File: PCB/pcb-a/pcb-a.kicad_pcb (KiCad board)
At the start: 2 copper layers, 89.4 x 42.2 mm, 28 parts, among them J1 Conn_02x05_Counter_Clockwise, J2 Conn_02x05_Counter_Clockwise, Q3 BC337, SW1 config, U1 ESP32-S2-DevKitM, U3 L7805

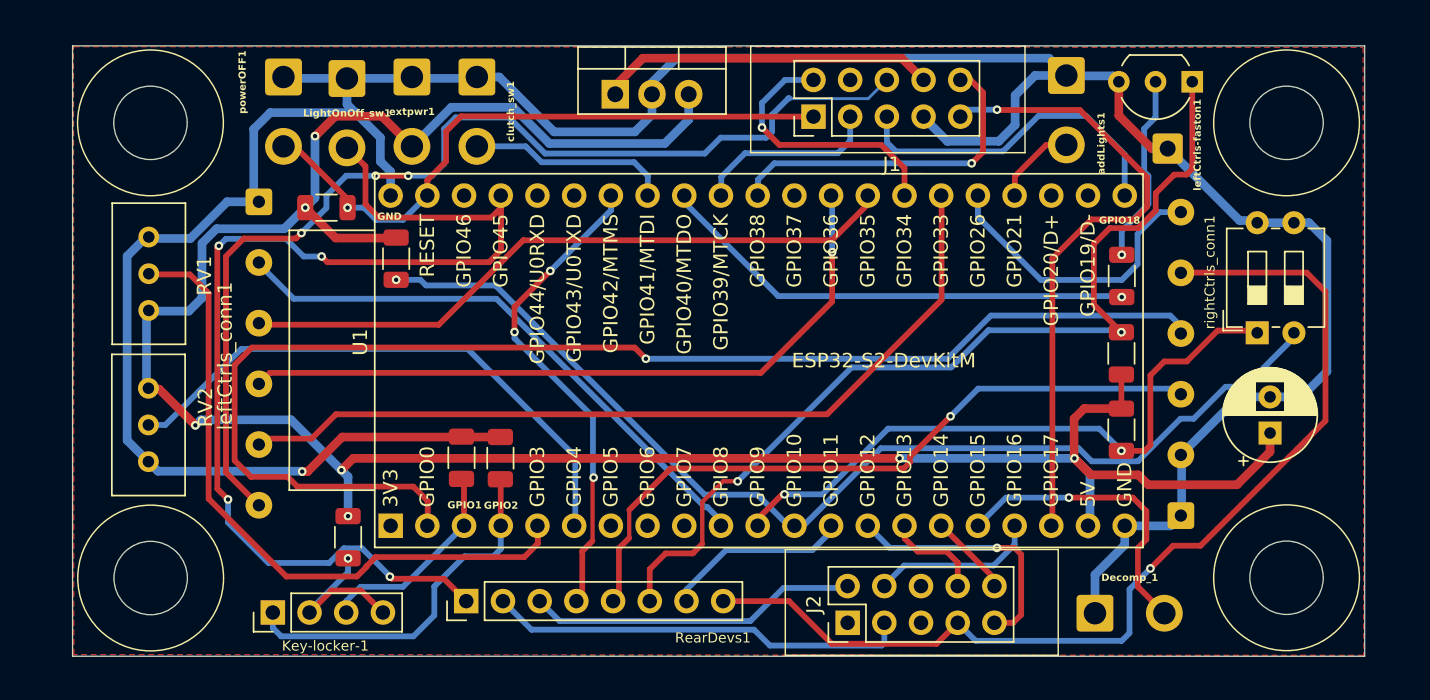
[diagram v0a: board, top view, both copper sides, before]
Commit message: Fixes and changes
- 8pin pin-header connectors have been replaced with more standard 10pin connectors
- Wrong components sizes have been fixed
- too small solder-wire connectors have been fixed
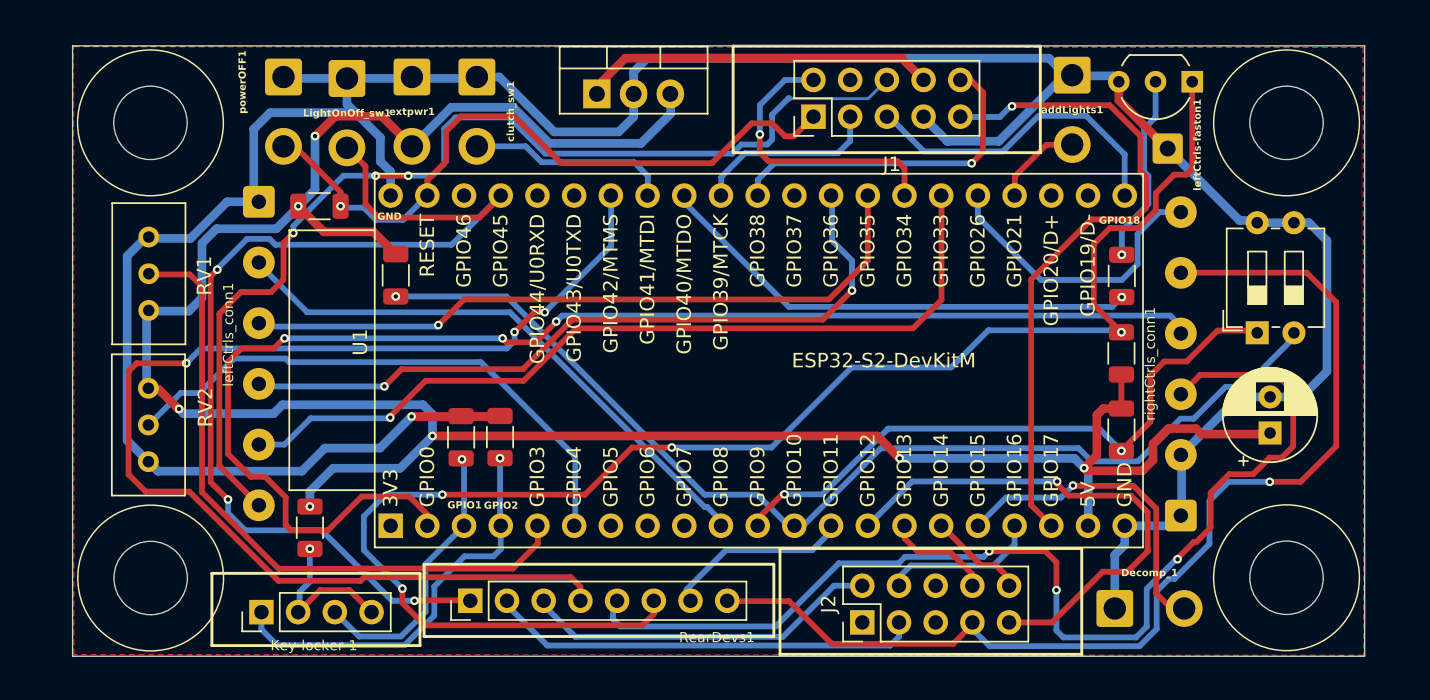
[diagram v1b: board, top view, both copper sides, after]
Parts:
- leftCtrls_conn1, rightCtrls_conn1: footprint Connector_Wire:SolderWire-0.25sqmm_1x06_P4.2mm_D0.65mm_OD1.7mm -> Custom_conn_wire:SolderWire-0.25sqmm_1x06_P4.2mm_D1.0mm_OD2.2mm
- moved R1 2.72 mm to (128.9, 95.5)
- moved R4 1.46 mm to (142.1, 89.2)
- moved R3 1.42 mm to (139.4, 89.2)
- moved Decomp_1 1.41 mm to (184.6, 101.1)
- moved U3 1.27 mm to (148.8, 65.4)
- moved R5 1.15 mm to (134.9, 78.0)
- moved J2 1.02 mm to (167.2, 102.0)
- moved Key-locker-1 0.79 mm to (125.6, 101.3)
- moved R2 0.49 mm to (129.6, 73.2)
- moved addLights1 0.41 mm to (181.7, 64.2)
- moved RearDevs1 0.28 mm to (140.0, 100.5)
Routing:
- net i_bykeStand: track 33.7 -> 83.7 mm
- net c_startEngine: track 66.0 -> 106.8 mm, vias 2 -> 4
- net c_brakeSwitch: track 48.8 -> 77.1 mm, vias 1 -> 3
- net o_keepAlive: track 17.7 -> 36.4 mm
- net i_Vx1: track 14.4 -> 19.7 mm, vias 0 -> 1
- net c_rearLight: track 78.9 -> 73.8 mm, vias 4 -> 3
- net 5V: track 167.3 -> 172.0 mm
- net c_engineOFF: track 71.8 -> 75.8 mm
- net i_powerOFF: track 44.5 -> 48.1 mm
- net i_Vx2: track 25.6 -> 28.5 mm, vias 0 -> 1
- net i_startButton: track 91.0 -> 93.8 mm, vias 1 -> 3
- net o_upLight: track 43.7 -> 46.4 mm
- net i_downLight: track 46.2 -> 48.6 mm, vias 0 -> 1
- net c_rightArrow: track 22.9 -> 24.7 mm
- net i_upLight: track 49.4 -> 51.1 mm, vias 1 -> 2
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
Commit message: hanges and fix
- The R6 and R8 pull-up resistors have been removed. I will use internal ones
- The J2 connector position has been moved
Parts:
- removed R5, R8: 100K, Resistor_SMD:R_1206_3216Metric
- moved Decomp_1 1.46 mm to (185.1, 102.4)
- moved J2 0.38 mm to (167.2, 102.4)
- moved Key-locker-1 0.31 mm to (125.9, 101.3)
- moved RearDevs1 0.25 mm to (140.3, 100.5)
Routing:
- net Net-(U1-GPIO10/TOUCH10/ADC1_CH9/FSPICS0/FSPIIO4): track 75.2 -> 41.7 mm, vias 1 -> 0
- net 5V: track 172.0 -> 163.6 mm
- net c_brakeSwitch: track 77.1 -> 69.1 mm
- net GND: track 206.9 -> 208.5 mm
- net c_engineOFF: track 75.8 -> 74.2 mm, vias 1 -> 2
- net i_decompr: track 23.0 -> 24.2 mm
- net o_keepAlive: track 36.4 -> 37.4 mm
- net Net-(U1-GPIO9/TOUCH9/ADC1_CH8/FSPIHD): track 43.8 -> 42.9 mm, vias 2 -> 0
- net i_Vx2: track 28.5 -> 29.2 mm
- net i_Vx1: track 19.7 -> 20.4 mm
- net c_leftArrow: track 29.8 -> 30.5 mm
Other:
- board size 89.4 x 42.2 mm -> 89.4 x 42.8 mm

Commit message: Small fixes...
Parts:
- moved C1 1.97 mm to (197.3, 89.1)
- moved SW1 1.27 mm to (195.8, 82.0)
- moved rightCtrls_conn1 0.61 mm to (189.8, 94.6)
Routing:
- net c_brakeSwitch: track 69.1 -> 72.9 mm
- net 5V: track 163.6 -> 165.6 mm
- net Net-(U1-GPIO10/TOUCH10/ADC1_CH9/FSPICS0/FSPIIO4): track 41.7 -> 43.3 mm
- net GND: track 208.5 -> 209.6 mm
- net i_engineON: track 20.5 -> 21.1 mm
- net o_keepAlive: track 37.4 -> 36.8 mm
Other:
- board size 89.4 x 42.8 mm -> 89.4 x 43.5 mm

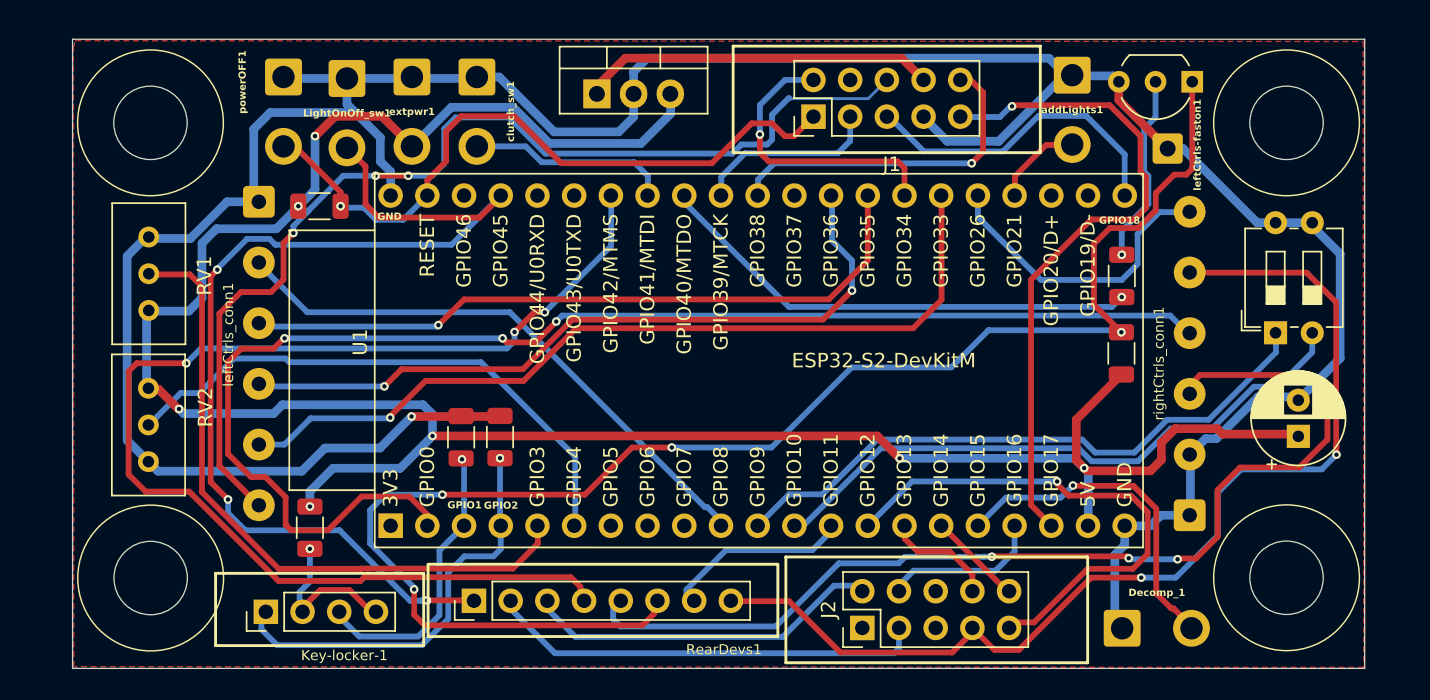
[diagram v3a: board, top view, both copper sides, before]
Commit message: PCBs sizes adjustment to be mounted as totem
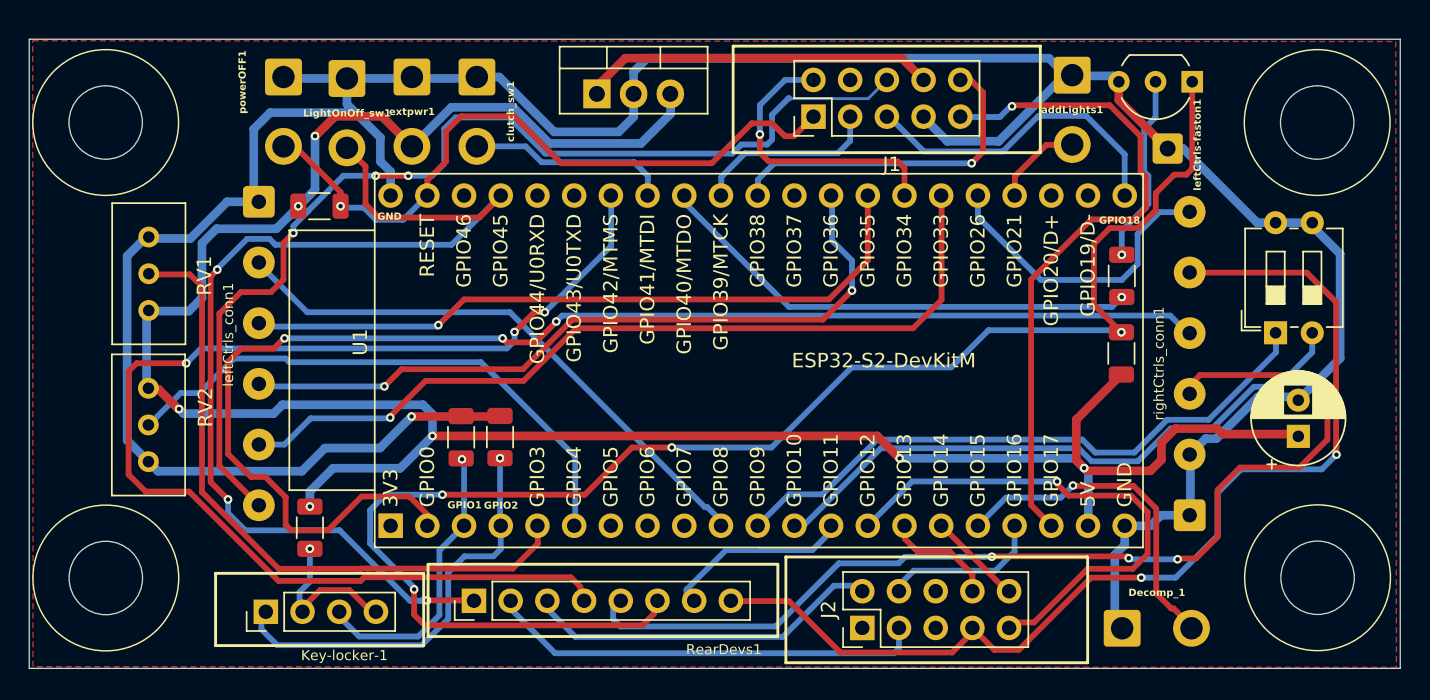
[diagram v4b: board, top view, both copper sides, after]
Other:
- board size 89.4 x 43.5 mm -> 94.9 x 43.5 mm
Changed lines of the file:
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@@
 	)
 	(gr_circle
-		(center 117.906315 67.45)
-		(end 122.95 67.45)
+		(center 114.805085 67.4266)
+		(end 119.84877 67.4266)
 		(stroke
 			(width 0.1)
@@
 	)
 	(gr_circle
-		(center 117.918685 98.95)
-		(end 122.96237 98.95)
+		(center 114.815933 98.947978)
+		(end 119.859618 98.947978)
 		(stroke
 			(width 0.1)
@@
 	)
 	(gr_circle
-		(center 196.524933 67.45)
-		(end 201.568618 67.45)
+		(center 198.646915 67.4266)
+		(end 203.6906 67.4266)
 		(stroke
 			(width 0.1)
@@
 	)
 	(gr_circle
-		(center 196.525 98.931315)
-		(end 201.568685 98.931315)
+		(center 198.672315 98.931315)
+		(end 203.716 98.931315)
 		(stroke
 			(width 0.1)
@@
 	)
 	(gr_circle
-		(center 117.918752 98.95)
-		(end 120.458752 98.939435)
+		(center 114.816 98.947978)
+		(end 117.356 98.937413)
 		(stroke
 			(width 0.05)
@@
 	)
 	(gr_circle
-		(center 196.525067 98.931315)
-		(end 199.065067 98.92075)
+		(center 198.672382 98.931315)
+		(end 201.212382 98.92075)
 		(stroke
 			(width 0.05)
@@
 	)
 	(gr_circle
-		(center 117.906382 67.45)
-		(end 120.446382 67.439435)
+		(center 114.805152 67.4266)
+		(end 117.345152 67.416035)
 		(stroke
 			(width 0.05)
@@
 	)
 	(gr_circle
-		(center 196.525 67.45)
-		(end 199.065 67.439435)
+		(center 198.646982 67.4266)
+		(end 201.186982 67.416035)
 		(stroke
 			(width 0.05)
@@
 	)
 	(gr_rect
-		(start 112.515 61.6648)
-		(end 201.933 105.2022)
+		(start 109.5178 61.6648)
+		(end 204.3968 105.2022)
 		(stroke
 			(width 0.05)
@@
 		(layer "B.Mask")
 		(pts
-			(xy 112.515 62.122) (xy 201.933 62.122)
+			(xy 198.672382 98.931315) (xy 114.816 98.947978)
+		)
+		(height -11.349584)
+		(format
+			(prefix "")
+			(suffix "")
+			(units 3)
+			(units_format 1)
+			(precision 4)
+		)
+		(style
+			(thickness 0.1)
+			(arrow_length 1.27)
+			(text_position_mode 0)
+			(arrow_direction outward)
+			(extension_height 0.58642)
+			(extension_offset 0.5)
+			(keep_text_aligned yes)
+		)
+		(gr_text "83,8564 mm"
+			(at 156.746217 109.139231 0.01138585799)
+			(layer "B.Mask")
+			(effects
+				(font
+					(size 1 1)
+					(thickness 0.15)
+				)
+			)
+		)
+	)
+	(dimension
+		(type aligned)
+		(layer "B.Mask")
+		(pts
+			(xy 109.75368 61.767957) (xy 204.079414 61.6648)
 		)
 		(height -3.941)
@@
 			(keep_text_aligned yes)
 		)
-		(gr_text "89,4180 mm"
-			(at 157.224 57.031 0)
+		(gr_text "94,3258 mm"
+			(at 156.910979 56.625381 0.06266069095)
 			(layer "B.Mask")
 			(effects
@@
 		(layer "B.Mask")
 		(pts
-			(xy 117.906315 67.475) (xy 117.925 98.956315)
+			(xy 114.805085 67.4266) (xy 114.816 98.947978)
 		)
 		(height 9.657589)
@@
 			(keep_text_aligned yes)
 		)
-		(gr_text "31,4813 mm"
-			(at 109.408071 83.220707 270.0340084)
+		(gr_text "31,5214 mm"
+			(at 106.302955 83.190235 270.0198418)
 			(layer "B.Mask")
 			(effects
@@
 		(layer "B.Mask")
 		(pts
-			(xy 201.933 105.2022) (xy 201.933 61.6648)
+			(xy 204.3968 105.2022) (xy 204.3968 61.6648)
 		)
 		(height 6.566213)
@@
 		)
 		(gr_text "43,5374 mm"
-			(at 207.349213 83.4335 90)
+			(at 209.813013 83.4335 90)
 			(layer "B.Mask")
 			(effects
@@
 		(polygon
 			(pts
-				(xy 112.701348 61.769609) (xy 201.824518 61.819551) (xy 201.875988 105.131884) (xy 112.600496 105.081884)
-				(xy 112.575 62.275)
+				(xy 109.75368 61.767957) (xy 204.079414 61.820814) (xy 204.130884 105.133147) (xy 109.779476 105.080304)
+				(xy 109.75368 61.767957)
 			)
 		)

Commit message: Wires to welded has been substituted bt pin-header connectors
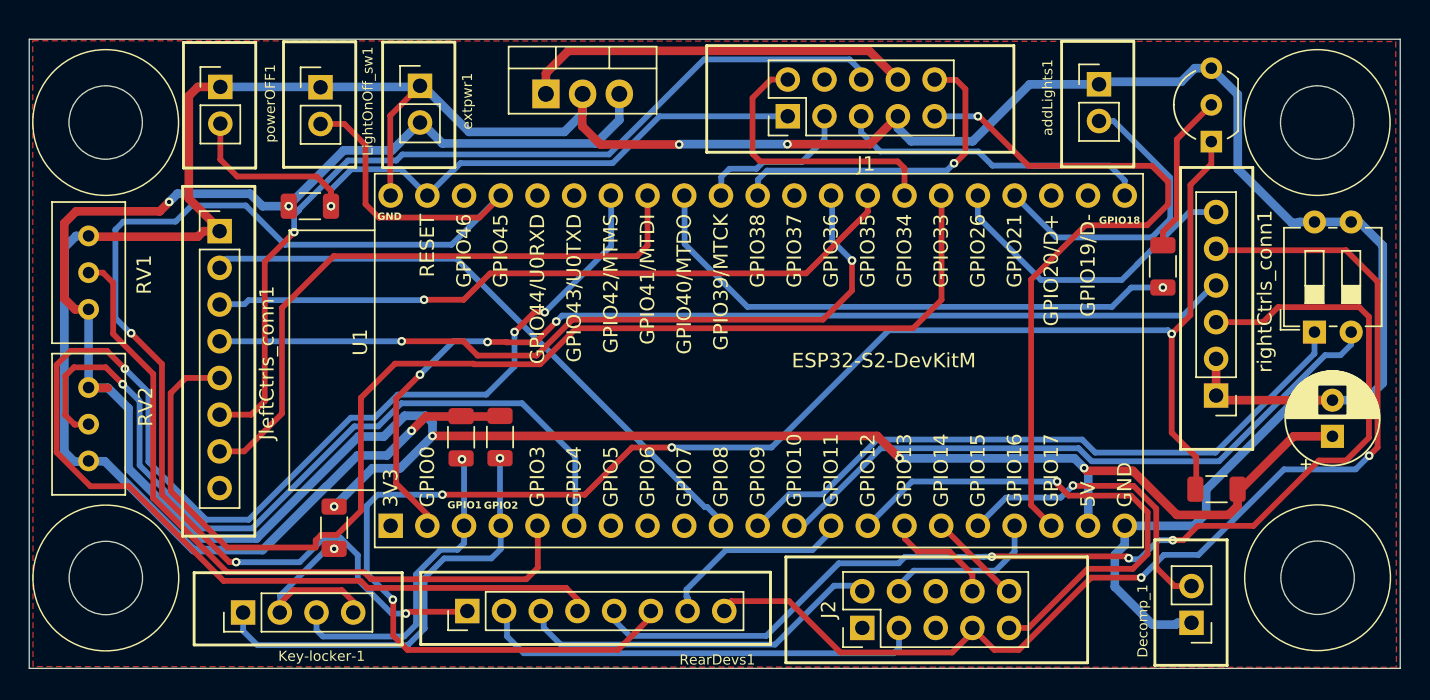
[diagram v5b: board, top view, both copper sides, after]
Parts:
- removed clutch_sw1: Conn_01x02, Connector_Wire:SolderWire-0.75sqmm_1x02_P4.8mm_D1.25mm_OD2.3mm
- removed leftCtrls-faston1: Conn_01x01, Connector_Wire:SolderWire-0.5sqmm_1x01_D0.9mm_OD2.1mm
- removed leftCtrls_conn1: Conn_01x06, Custom_conn_wire:SolderWire-0.25sqmm_1x06_P4.2mm_D1.0mm_OD2.2mm
- added JleftCtrls_conn1: Conn_01x08, Connector_PinHeader_2.54mm:PinHeader_1x08_P2.54mm_Vertical, F.Cu at (122.7, 74.9)
- Decomp_1, LightOnOff_sw1, addLights1, extpwr1, powerOFF1: footprint Connector_Wire:SolderWire-0.75sqmm_1x02_P4.8mm_D1.25mm_OD2.3mm -> Connector_PinHeader_2.54mm:PinHeader_1x02_P2.54mm_Vertical
- rightCtrls_conn1: footprint Custom_conn_wire:SolderWire-0.25sqmm_1x06_P4.2mm_D1.0mm_OD2.2mm -> Connector_PinHeader_2.54mm:PinHeader_1x06_P2.54mm_Vertical
- moved R6 11.5 mm to (191.7, 92.8), turned to 0 degrees
- moved rightCtrls_conn1 8.48 mm to (191.7, 86.3), turned to 180 degrees
- moved Decomp_1 4.82 mm to (189.9, 102.0), turned to 180 degrees
- moved powerOFF1 4.42 mm to (122.7, 65.0), turned to 0 degrees
- moved Q3 4.35 mm to (191.3, 68.7), turned to 90 degrees
- moved RV1 4.17 mm to (113.6, 75.3)
- moved RV2 4.14 mm to (113.6, 85.8)
- moved U3 3.53 mm to (145.3, 65.4)
- moved R7 2.92 mm to (188.0, 77.4)
- moved SW1 2.69 mm to (198.5, 81.9)
- moved C1 2.36 mm to (199.7, 89.1)
- moved addLights1 1.96 mm to (183.5, 64.8), turned to 0 degrees
- moved LightOnOff_sw1 1.93 mm to (129.7, 65.0), turned to 0 degrees
- moved J1 1.78 mm to (162.0, 67.0)
- moved R1 1.68 mm to (130.6, 95.5)
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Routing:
- net i_clutch: track 14.0 -> 43.3 mm
- net GND: track 209.6 -> 236.9 mm, vias 1 -> 3
- net i_rightArrow: track 58.7 -> 84.8 mm, vias 1 -> 0
- net i_startButton: track 93.8 -> 69.8 mm
- net i_bykeStand: track 83.8 -> 106.4 mm
- net c_rearLight: track 74.1 -> 94.9 mm
- net Net-(U1-GPIO4/TOUCH4/ADC1_CH3): track 39.1 -> 57.3 mm, vias 0 -> 1
- net i_addLight: track 6.79 -> 22.0 mm
- net c_horn: track 73.6 -> 61.9 mm, vias 3 -> 1
- net c_startEngine: track 106.5 -> 116.1 mm
- net 5V: track 165.6 -> 174.7 mm, vias 7 -> 6
- net c_brakeSwitch: track 72.9 -> 78.9 mm
- net o_startEngine: track 33.6 -> 38.4 mm
- net Net-(U1-GPIO3/TOUCH3/ADC1_CH2): track 46.2 -> 50.7 mm
- net c_engineOFF: track 74.3 -> 78.0 mm
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
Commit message: More space to the ESP32's USB cable connector
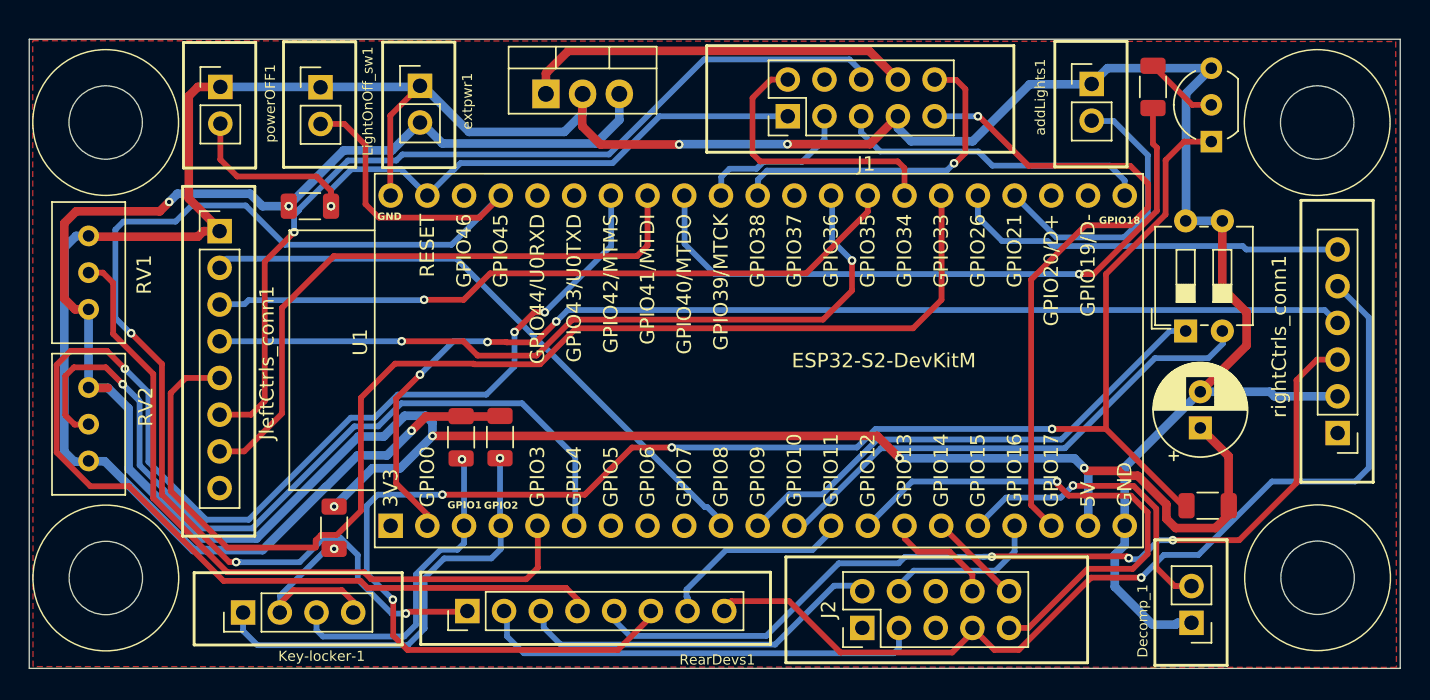
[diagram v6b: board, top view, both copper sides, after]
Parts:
- moved R7 12.4 mm to (187.3, 65.0)
- moved C1 9.16 mm to (190.6, 88.6)
- moved SW1 8.92 mm to (189.5, 81.9)
- moved rightCtrls_conn1 8.80 mm to (200.1, 88.9)
- moved R6 1.30 mm to (191.1, 93.9)
- moved addLights1 0.51 mm to (183.0, 64.8)
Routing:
- net c_brakeSwitch: track 78.9 -> 63.5 mm
- net GND: track 236.9 -> 222.2 mm
- net c_engineOFF: track 78.0 -> 66.7 mm, vias 2 -> 1
- net Net-(U1-GPIO9/TOUCH9/ADC1_CH8/FSPIHD): track 46.2 -> 35.7 mm
- net Net-(U1-GPIO10/TOUCH10/ADC1_CH9/FSPICS0/FSPIIO4): track 45.8 -> 36.2 mm
- net i_startButton: track 69.8 -> 77.8 mm
- net o_startEngine: track 38.4 -> 45.5 mm
- net Net-(Q3-B): track 11.1 -> 5.16 mm
- net i_engineON: track 21.7 -> 27.3 mm
- net o_upLight: track 48.8 -> 46.1 mm
- net 5V: track 174.7 -> 172.8 mm
- net i_addLight: track 22.0 -> 20.1 mm
- net c_startEngine: track 116.1 -> 114.5 mm
